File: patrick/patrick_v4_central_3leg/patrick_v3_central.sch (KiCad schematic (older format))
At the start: 12 parts, among them J1 Conn_02x05_Counter_Clockwise, J10 61300311121, J4 Conn_02x05_Counter_Clockwise, J5 Conn_02x05_Counter_Clockwise, J7 61300211121, J9 61300211121, U1 ZLDO1117G33TA, U3 BL652-SA-01

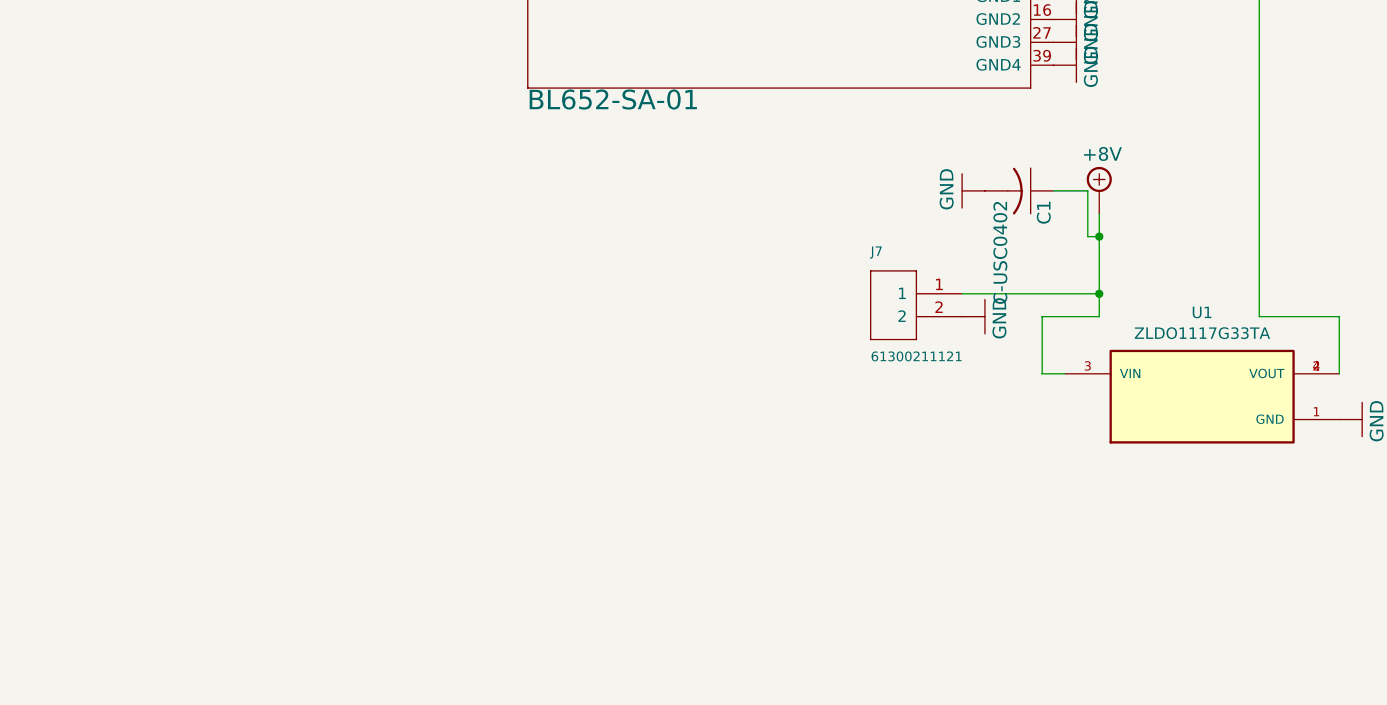
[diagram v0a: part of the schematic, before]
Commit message: added IMU to 3 legged circuit
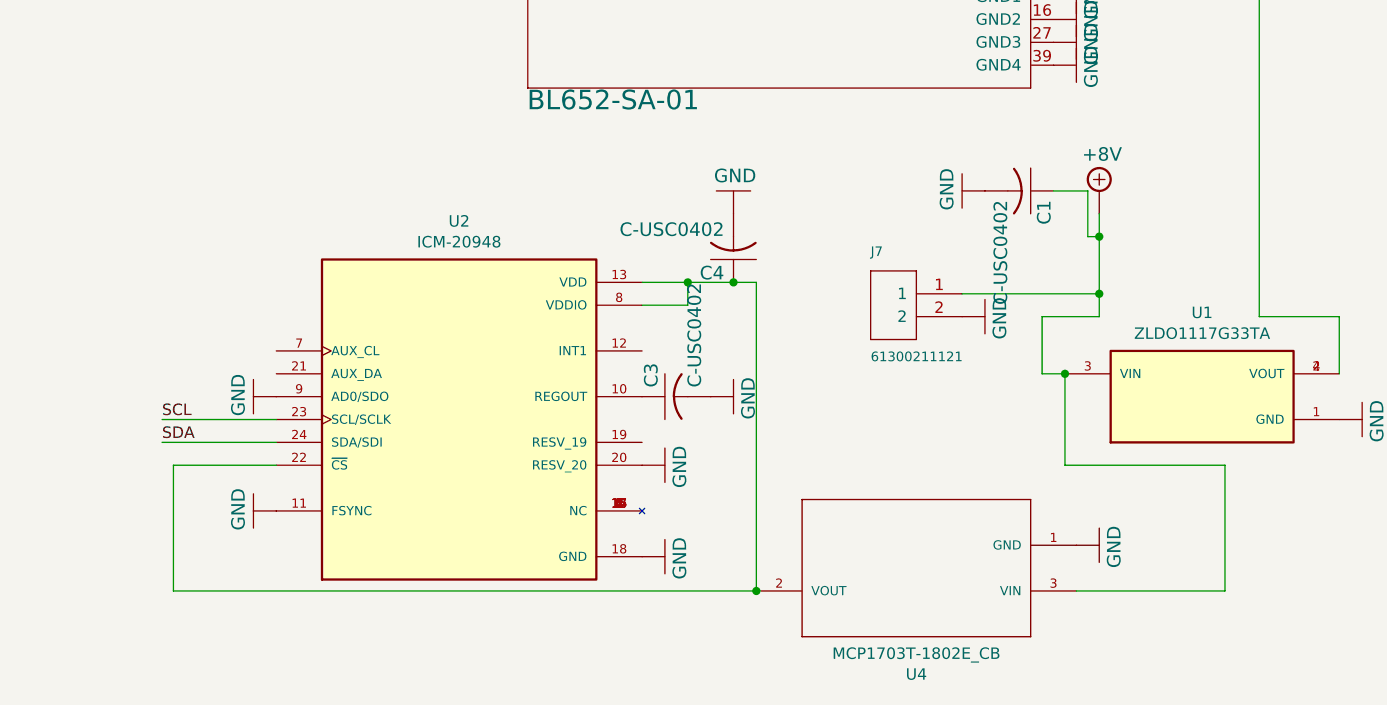
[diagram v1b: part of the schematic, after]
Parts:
- added C3, C4: C-USC0402, Capacitor_SMD:C_0402_1005Metric_Pad0.74x0.62mm_HandSolder, symbol patrick_0.5-eagle-import:C-USC0402
- added U2: ICM-20948, ICM-20948:QFN40P300X300X105-24N, symbol ICM-20948:ICM-20948
- added U4: MCP1703T-1802E_CB, MCP1703T-1802E_CB:SOT95P255X145-3N, symbol MCP1703T-1802E_CB:MCP1703T-1802E_CB
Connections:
- wire segments 64 -> 79
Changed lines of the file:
@@
 Wire Wire Line
 	14800 2700 13900 2700
-Wire Wire Line
-	15300 3100 14800 3100
-Connection ~ 15300 3100
 Connection ~ 14800 3100
 Text Label 14900 3100 0    70   ~ 0
@@
 $EndComp
 $Comp
-L patrick_0.5-eagle-import:C-USC0402 C2
-U 1 1 733CA19D
-P 15300 3200
-F 0 "C2" H 15340 3225 59  0000 L BNN
-F 1 "C-USC0402" H 15340 3035 59  0000 L BNN
-F 2 "Capacitor_SMD:C_0402_1005Metric_Pad0.74x0.62mm_HandSolder" H 15300 3200 50  0001 C CNN
-F 3 "" H 15300 3200 50  0001 C CNN
-	1    15300 3200
-	1    0    0    -1
-$EndComp
-$Comp
-L patrick_0.5-eagle-import:GND #GND028
-U 1 1 0345B4CC
-P 15300 3500
-F 0 "#GND028" H 15300 3500 50  0001 C CNN
-F 1 "GND" H 15200 3400 59  0000 L BNN
-F 2 "" H 15300 3500 50  0001 C CNN
-F 3 "" H 15300 3500 50  0001 C CNN
-	1    15300 3500
-	1    0    0    -1
-$EndComp
-$Comp
 L patrick_0.5-eagle-import:61300211121 J7
 U 1 1 1B1E17EB
@@
 	1    0    0    -1
 $EndComp
-Wire Wire Line
-	15300 3100 15700 3100
 $Comp
 L patrick_0.5-eagle-import:BL652-SA-01 U3
@@
 Wire Wire Line
 	16050 6900 16050 7150
+$Comp
+L patrick_0.5-eagle-import:GND #GND0101
+U 1 1 617A4001
+P 13100 7950
+F 0 "#GND0101" H 13100 7950 50  0001 C CNN
+F 1 "GND" H 13000 7850 59  0000 L BNN
+F 2 "" H 13100 7950 50  0001 C CNN
+F 3 "" H 13100 7950 50  0001 C CNN
+	1    13100 7950
+	0    -1   -1   0
+$EndComp
+$Comp
+L MCP1703T-1802E_CB:MCP1703T-1802E_CB U4
+U 1 1 617ABE6D
+P 14900 8100
+F 0 "U4" H 15600 8465 50  0000 C CNN
+F 1 "MCP1703T-1802E_CB" H 15600 8374 50  0000 C CNN
+F 2 "MCP1703T-1802E_CB:SOT95P255X145-3N" H 14900 8100 50  0001 L BNN
+F 3 "" H 14900 8100 50  0001 L BNN
+F 4 "1439516" H 14900 8100 50  0001 L BNN "OC_FARNELL"
+F 5 "MICROCHIP" H 14900 8100 50  0001 L BNN "SUPPLIER"
+F 6 "MCP1703T-1802E/CB" H 14900 8100 50  0001 L BNN "MPN"
+F 7 "SOT23-3" H 14900 8100 50  0001 L BNN "PACKAGE"
+F 8 "58M8874" H 14900 8100 50  0001 L BNN "OC_NEWARK"
+	1    14900 8100
+	-1   0    0    1
+$EndComp
+$Comp
+L patrick_0.5-eagle-import:GND #GND0102
+U 1 1 617AEF88
+P 15000 7900
+F 0 "#GND0102" H 15000 7900 50  0001 C CNN
+F 1 "GND" H 14900 7800 59  0000 L BNN
+F 2 "" H 15000 7900 50  0001 C CNN
+F 3 "" H 15000 7900 50  0001 C CNN
+	1    15000 7900
+	0    -1   -1   0
+$EndComp
+Wire Wire Line
+	14900 8100 15550 8100
+Wire Wire Line
+	15550 8100 15550 7550
+Wire Wire Line
+	15550 7550 14850 7550
+Wire Wire Line
+	14850 7550 14850 7150
+Connection ~ 14850 7150
+$Comp
+L patrick_0.5-eagle-import:GND #GND028
+U 1 1 0345B4CC
+P 15300 3500
+F 0 "#GND028" H 15300 3500 50  0001 C CNN
+F 1 "GND" H 15200 3400 59  0000 L BNN
+F 2 "" H 15300 3500 50  0001 C CNN
+F 3 "" H 15300 3500 50  0001 C CNN
+	1    15300 3500
+	1    0    0    -1
+$EndComp
+Wire Wire Line
+	15300 3100 15700 3100
+Wire Wire Line
+	15300 3100 14800 3100
+Connection ~ 15300 3100
+$Comp
+L patrick_0.5-eagle-import:C-USC0402 C2
+U 1 1 733CA19D
+P 15300 3200
+F 0 "C2" H 15340 3225 59  0000 L BNN
+F 1 "C-USC0402" H 15340 3035 59  0000 L BNN
+F 2 "Capacitor_SMD:C_0402_1005Metric_Pad0.74x0.62mm_HandSolder" H 15300 3200 50  0001 C CNN
+F 3 "" H 15300 3200 50  0001 C CNN
+	1    15300 3200
+	1    0    0    -1
+$EndComp
+$Comp
+L patrick_0.5-eagle-import:C-USC0402 C4
+U 1 1 617BA106
+P 13400 6650
+F 0 "C4" H 13440 6675 59  0000 L BNN
+F 1 "C-USC0402" H 13440 6485 59  0000 L BNN
+F 2 "Capacitor_SMD:C_0402_1005Metric_Pad0.74x0.62mm_HandSolder" H 13400 6650 50  0001 C CNN
+F 3 "" H 13400 6650 50  0001 C CNN
+	1    13400 6650
+	-1   0    0    1
+$EndComp
+$Comp
+L patrick_0.5-eagle-import:GND #GND0107
+U 1 1 617BA10C
+P 13400 6350
+F 0 "#GND0107" H 13400 6350 50  0001 C CNN
+F 1 "GND" H 13300 6250 59  0000 L BNN
+F 2 "" H 13400 6350 50  0001 C CNN
+F 3 "" H 13400 6350 50  0001 C CNN
+	1    13400 6350
+	-1   0    0    1
+$EndComp
+$Comp
+L patrick_0.5-eagle-import:C-USC0402 C3
+U 1 1 617C30C0
+P 13100 7250
+F 0 "C3" H 13140 7275 59  0000 L BNN
+F 1 "C-USC0402" H 13140 7085 59  0000 L BNN
+F 2 "Capacitor_SMD:C_0402_1005Metric_Pad0.74x0.62mm_HandSolder" H 13100 7250 50  0001 C CNN
+F 3 "" H 13100 7250 50  0001 C CNN
+	1    13100 7250
+	0    -1   -1   0
+$EndComp
+$Comp
+L patrick_0.5-eagle-import:GND #GND0108
+U 1 1 617C30C6
+P 13400 7250
+F 0 "#GND0108" H 13400 7250 50  0001 C CNN
+F 1 "GND" H 13300 7150 59  0000 L BNN
+F 2 "" H 13400 7250 50  0001 C CNN
+F 3 "" H 13400 7250 50  0001 C CNN
+	1    13400 7250
+	0    -1   -1   0
+$EndComp
+$Comp
+L patrick_0.5-eagle-import:GND #GND0109
+U 1 1 617C5991
+P 13100 7550
+F 0 "#GND0109" H 13100 7550 50  0001 C CNN
+F 1 "GND" H 13000 7450 59  0000 L BNN
+F 2 "" H 13100 7550 50  0001 C CNN
+F 3 "" H 13100 7550 50  0001 C CNN
+	1    13100 7550
+	0    -1   -1   0
+$EndComp
+Wire Wire Line
+	11400 7350 10900 7350
+Text Label 10900 7350 0    50   ~ 0
+SCL
+Text Label 10900 7450 0    50   ~ 0
+SDA
+Wire Wire Line
+	11400 7450 10900 7450
+Wire Wire Line
+	13000 6750 13200 6750
+Wire Wire Line
+	13500 6750 13500 8100
+Wire Wire Line
+	13000 6850 13200 6850
+Wire Wire Line
+	13200 6850 13200 6750
+Connection ~ 13200 6750
+Wire Wire Line
+	13200 6750 13400 6750
+Connection ~ 13400 6750
+Wire Wire Line
+	13400 6750 13500 6750
+$Comp
+L patrick_0.5-eagle-import:GND #GND0110
+U 1 1 6180295F
+P 11300 7750
+F 0 "#GND0110" H 11300 7750 50  0001 C CNN
+F 1 "GND" H 11200 7650 59  0000 L BNN
+F 2 "" H 11300 7750 50  0001 C CNN
+F 3 "" H 11300 7750 50  0001 C CNN
+	1    11300 7750
+	0    1    1    0
+$EndComp
+$Comp
+L patrick_0.5-eagle-import:GND #GND0111
+U 1 1 61804FBA
+P 11300 7250
+F 0 "#GND0111" H 11300 7250 50  0001 C CNN
+F 1 "GND" H 11200 7150 59  0000 L BNN
+F 2 "" H 11300 7250 50  0001 C CNN
+F 3 "" H 11300 7250 50  0001 C CNN
+	1    11300 7250
+	0    1    1    0
+$EndComp
+$Comp
+L ICM-20948:ICM-20948 U2
+U 1 1 6180B418
+P 12200 7350
+F 0 "U2" H 12200 8217 50  0000 C CNN
+F 1 "ICM-20948" H 12200 8126 50  0000 C CNN
+F 2 "ICM-20948:QFN40P300X300X105-24N" H 12200 7350 50  0001 L BNN
+F 3 "" H 12200 7350 50  0001 L BNN
+F 4 "IPC 7351B" H 12200 7350 50  0001 L BNN "STANDARD"
+F 5 "TDK InvenSense" H 12200 7350 50  0001 L BNN "MANUFACTURER"
+F 6 "1.3" H 12200 7350 50  0001 L BNN "PARTREV"
+F 7 "1.05 mm" H 12200 7350 50  0001 L BNN "MAXIMUM_PACKAGE_HEIGHT"
+	1    12200 7350
+	1    0    0    -1
+$EndComp
+Wire Wire Line
+	11400 7550 10950 7550
+Wire Wire Line
+	10950 7550 10950 8100
+Wire Wire Line
+	10950 8100 13500 8100
+Connection ~ 13500 8100
 $EndSCHEMATC
